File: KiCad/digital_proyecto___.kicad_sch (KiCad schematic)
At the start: 44 parts, among them J10 DE9_Pins, J11 DE9_Pins, U1 74AHCT1G125, U10 MCP2561-E-MF, U11 MAX3232, U12 A1101xLH, U13 A1101xLH, U2 LM393, U3 LM393

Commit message: Cambio DG y pinzeladas ultimas al esquematico
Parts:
- J10, J11: footprint Connector_Dsub:DSUB-9_Socket_Horizontal_P2.77x2.84mm_EdgePinOffset4.94mm_Housed_MountingHolesOffset4.94mm -> Connector_Dsub:DSUB-9_Pins_Horizontal_P2.77x2.54mm_EdgePinOffset9.40mm
- U1: footprint (none) -> Package_TO_SOT_SMD:SOT-553
- U2, U3: footprint (none) -> Package_SO:SOIC-8_3.9x4.9mm_P1.27mm
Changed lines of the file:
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@@
 			)
 		)
-		(property "Footprint" "Connector_Dsub:DSUB-9_Socket_Horizontal_P2.77x2.84mm_EdgePinOffset4.94mm_Housed_MountingHolesOffset4.94mm"
+		(property "Footprint" "Connector_Dsub:DSUB-9_Pins_Horizontal_P2.77x2.54mm_EdgePinOffset9.40mm"
 			(at 96.52 54.61 0)
 			(effects
@@
 			)
 		)
-		(property "Footprint" ""
+		(property "Footprint" "Package_SO:SOIC-8_3.9x4.9mm_P1.27mm"
 			(at 224.79 88.9 0)
 			(effects
@@
 			)
 		)
-		(property "Footprint" ""
+		(property "Footprint" "Package_SO:SOIC-8_3.9x4.9mm_P1.27mm"
 			(at 224.79 48.26 0)
 			(effects
@@
 			)
 		)
-		(property "Footprint" "Connector_Dsub:DSUB-9_Socket_Horizontal_P2.77x2.84mm_EdgePinOffset4.94mm_Housed_MountingHolesOffset4.94mm"
+		(property "Footprint" "Connector_Dsub:DSUB-9_Pins_Horizontal_P2.77x2.54mm_EdgePinOffset9.40mm"
 			(at 30.48 133.35 0)
 			(effects
@@
 			)
 		)
-		(property "Footprint" ""
+		(property "Footprint" "Package_SO:SOIC-8_3.9x4.9mm_P1.27mm"
 			(at 224.79 106.68 0)
 			(effects
@@
 			)
 		)
-		(property "Footprint" ""
+		(property "Footprint" "Package_SO:SOIC-8_3.9x4.9mm_P1.27mm"
 			(at 224.79 66.04 0)
 			(effects
@@
 			)
 		)
-		(property "Footprint" ""
+		(property "Footprint" "Package_SO:SOIC-8_3.9x4.9mm_P1.27mm"
 			(at 280.67 96.52 0)
 			(effects
@@
 			)
 		)
-		(property "Footprint" ""
+		(property "Footprint" "Package_SO:SOIC-8_3.9x4.9mm_P1.27mm"
 			(at 280.67 55.88 0)
 			(effects
@@
 			)
 		)
-		(property "Footprint" ""
+		(property "Footprint" "Package_TO_SOT_SMD:SOT-553"
 			(at 204.47 146.05 0)
 			(effects

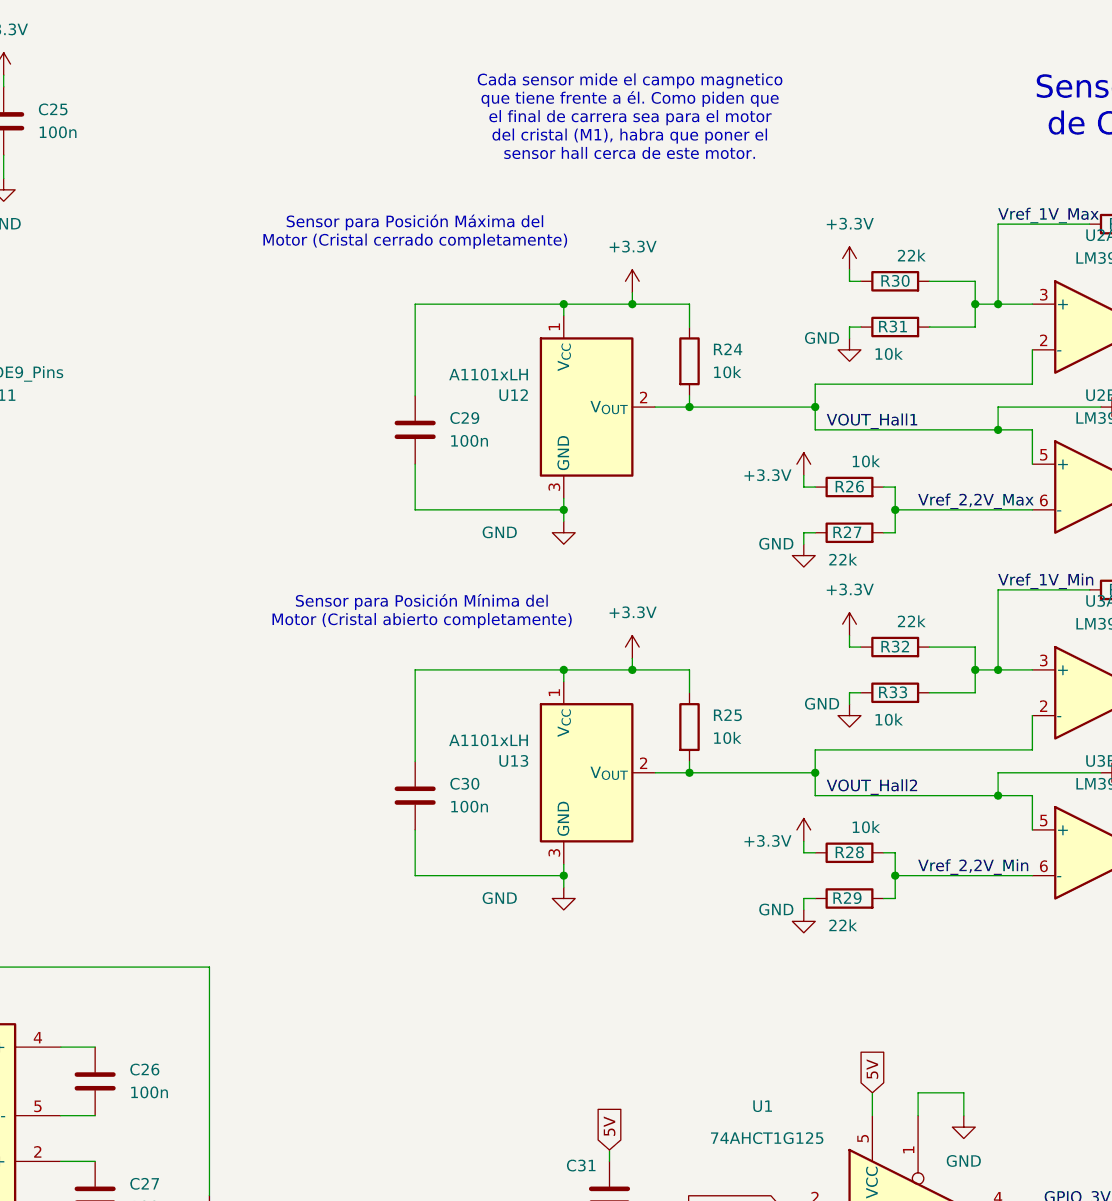
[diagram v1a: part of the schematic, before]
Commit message: pujo el esquematico a medio hacer despues de hacer cambios para mejorar el 2o layout
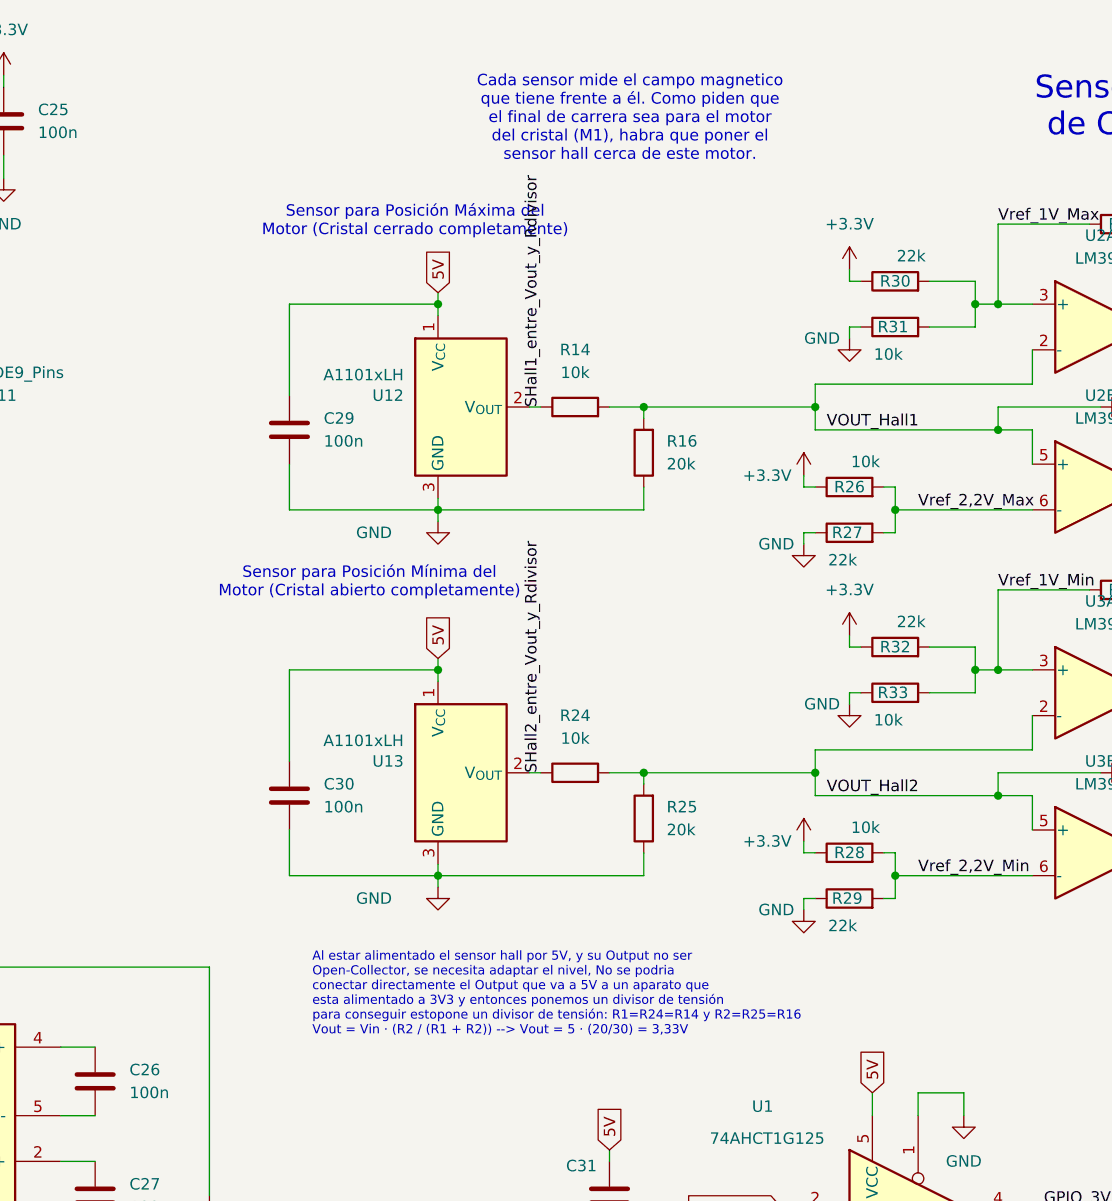
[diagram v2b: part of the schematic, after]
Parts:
- added R14: 10k, Resistor_SMD:R_0805_2012Metric, symbol Device:R
- added R16: 20k, Resistor_SMD:R_0805_2012Metric, symbol Device:R
- R25: value 10k -> 20k
- U1: footprint Package_TO_SOT_SMD:SOT-553 -> Package_TO_SOT_SMD:SOT-23-5_HandSoldering
- U11: footprint Package_SO:SSOP-16_5.3x6.2mm_P0.65mm -> Package_SO:SOIC-16_3.9x9.9mm_P1.27mm
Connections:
- net +3.3V: no longer C29.1, C30.1, R24.1, R25.1, U12.1 (V_{CC}), U13.1 (V_{CC})
- net 5V: now also C29.1, C30.1, U12.1 (V_{CC}), U13.1 (V_{CC})
- net GND: now also R25.1, R16.1
- net VOUT_Hall1: now also R14.2, R16.2; no longer R24.2, U12.2 (V_{OUT})
- net VOUT_Hall2: now also R24.2; no longer U13.2 (V_{OUT})
- new net SHall1_entre_Vout_y_Rdivisor: R14.1, U12.2 (V_{OUT})
- new net SHall2_entre_Vout_y_Rdivisor: R24.1, U13.2 (V_{OUT})
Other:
- note added: "Al estar alimentado el sensor hall por 5V, y su Output no ser Open-Collector, se necesita adaptar el nivel, No se podria conectar directamente el Output que va a 5V a un aparato que esta alimentado a 3V3 y entonces ponemos un divisor de tensión para conseguir estopone un divisor de tensión: R1=R24=R14 y R2=R25=R16 Vout = Vin · (R2 / (R1 + R2)) --> Vout = 5 · (20/30) = 3,33V"
- moved on the sheet: C29, C30, U12, U13

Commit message: Cambios Layout propuestos para mejorar posicionamiento
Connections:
- net C1+: now reaches C23.1, U11.1 (C1+)
- net VS+: now reaches C27.1, U11.2 (VS+)
- net C1-: now reaches C23.2, U11.3 (C1-)
- net C2+: now reaches C26.1, U11.4 (C2+)
- net C2-: now reaches C26.2, U11.5 (C2-)
- net VS-: now reaches C27.2, U11.6 (VS-)

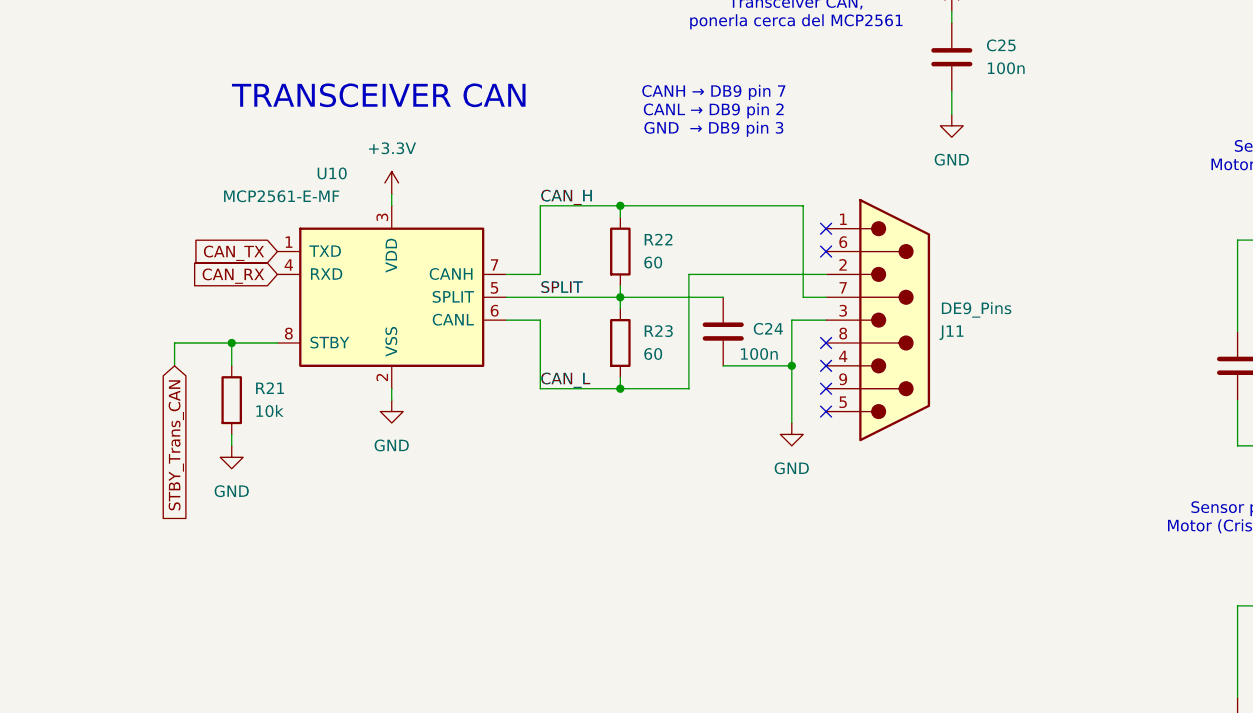
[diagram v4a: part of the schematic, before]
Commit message: PCB casi acabada, despues de revisión de ayer 27/04 y cambio en componente CAN, que se vera reflejado en README y en DB
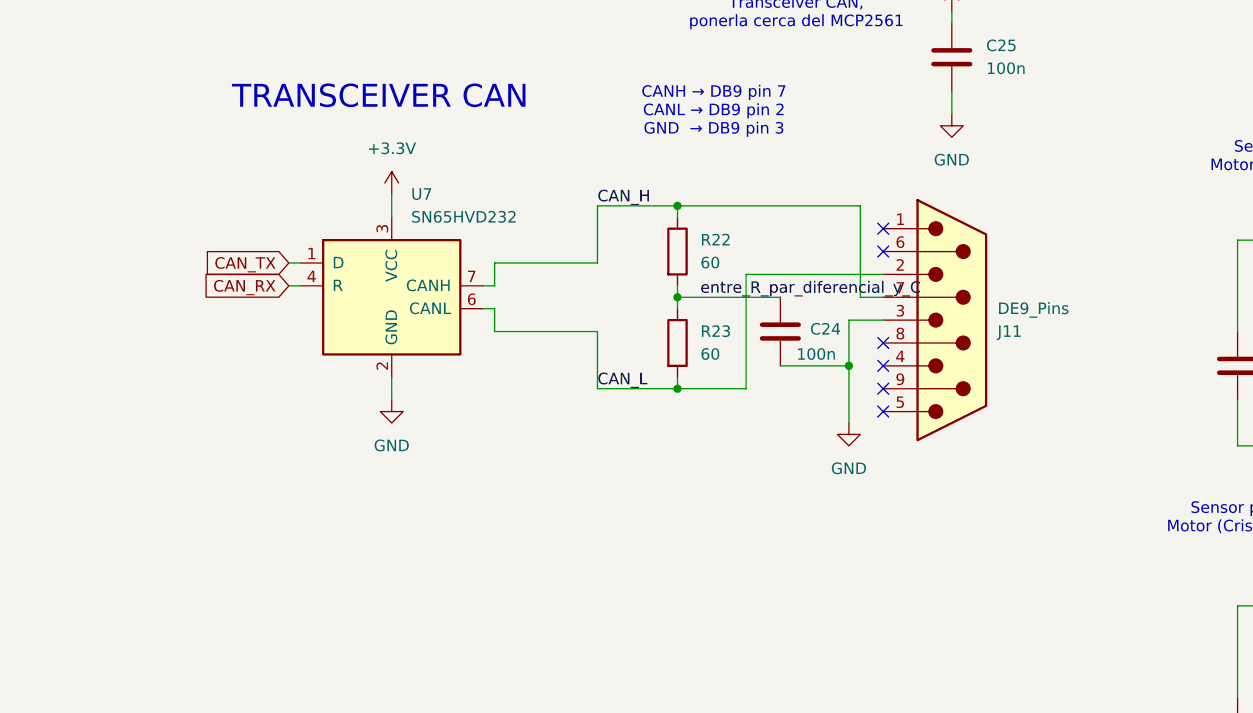
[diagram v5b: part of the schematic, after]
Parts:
- removed R21: 10k, Resistor_SMD:R_0805_2012Metric, symbol Device:R
- removed U10: MCP2561-E-MF, Package_SO:SOIC-8-1EP_3.9x4.9mm_P1.27mm_EP2.29x3mm, symbol Interface_CAN_LIN:MCP2561-E-MF
- added U7: SN65HVD232, Package_SO:SOIC-8_3.9x4.9mm_P1.27mm, symbol Interface_CAN_LIN:SN65HVD232
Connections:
- net +3.3V: now also U7.3 (VCC)
- net CAN_H: now also U7.7 (CANH)
- net CAN_L: now also U7.6 (CANL)
- net CAN_RX: now also U7.4 (R)
- net CAN_TX: now also U7.1 (D)
- net GND: now also U7.2 (GND)
- net SPLIT renamed entre_R_par_diferencial_y_C
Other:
- moved on the sheet: C24, J11, R22, R23

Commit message: Layout definitivo
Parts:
- removed C33: 100n, Capacitor_SMD:C_0805_2012Metric, symbol Device:C
- removed R24, R26, R28, R31, R33, R39, R40, R41, R42: 10k, Resistor_SMD:R_0805_2012Metric, symbol Device:R
- removed R25: 20k, Resistor_SMD:R_0805_2012Metric, symbol Device:R
- removed R27, R29, R30, R32: 22k, Resistor_SMD:R_0805_2012Metric, symbol Device:R
- removed R34, R35, R36, R37: 220k, Resistor_SMD:R_0805_2012Metric, symbol Device:R
- removed U2: LM393, Package_SO:SOIC-8_3.9x4.9mm_P1.27mm, symbol Comparator:LM393
- R16: value 20k -> 10k
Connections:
- net Vref_1V_Min is gone; now on net entre_sHall_R14: U3.3 (+)
- net Vref_2,2V_Min is gone; now on net Pos_MIN: U3.6 (-)
- net +3.3V: now also R14.1, R16.1
- net GND: no longer R16.1
- net DOWN_LOW_M1_Pos_Min renamed Pos_MAX
- net Pos_MAX: now also U3.2 (-)
- net HIGH_UP_M1_Pos_Min renamed Pos_MIN
- net SHall1_entre_Vout_y_Rdivisor renamed entre_sHall_R14
- net entre_sHall_R14: now also R14.2; no longer R14.1
- net SHall2_entre_Vout_y_Rdivisor renamed entre_sHall_R16
- net entre_sHall_R16: now also R16.2, U3.5 (+)
- removed net VOUT_Hall1: R14.2, R16.2
- removed net VOUT_Hall2: U3.2 (-), U3.5 (+)
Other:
- moved on the sheet: C34, U3B, U3C
